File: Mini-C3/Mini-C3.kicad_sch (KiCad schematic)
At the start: 9 parts, among them J1 TB_1X2, J2 Conn_01x03, J3 Conn_01x07, J4 Conn_01x02, SW1 SW_Push, U1 Driver Module, U2 ESP32-C3_SUPERMINI

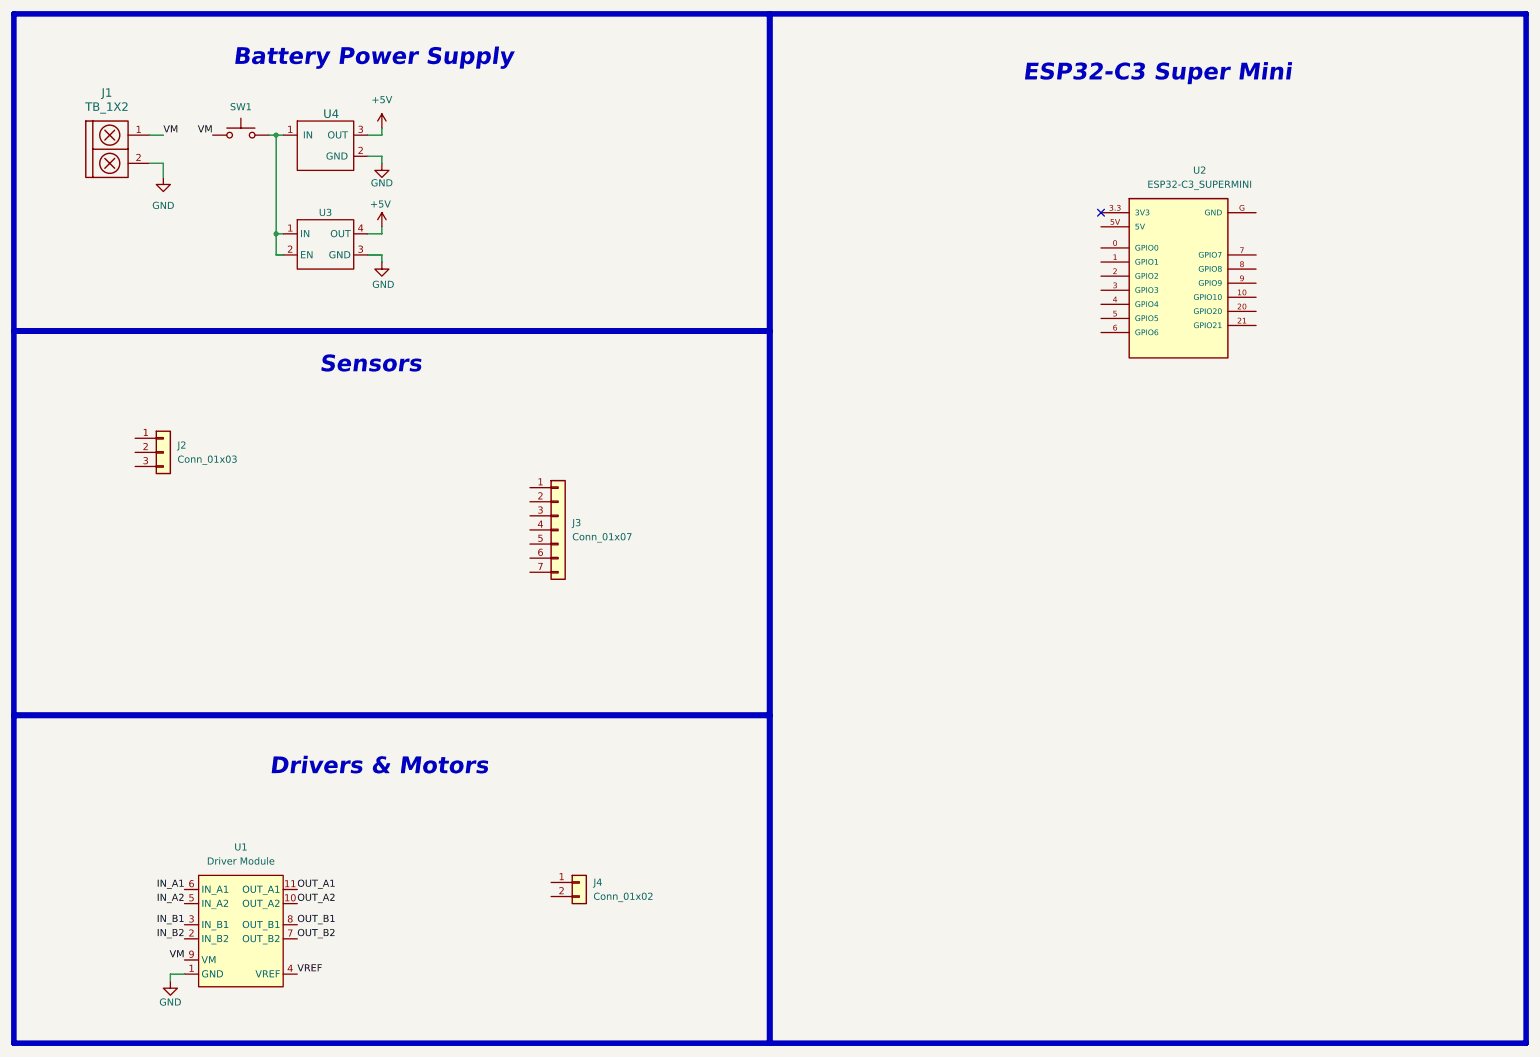
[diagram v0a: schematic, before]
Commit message: schematic & pcb
ESP32-C3 pinout img added. The schematic is almost done.
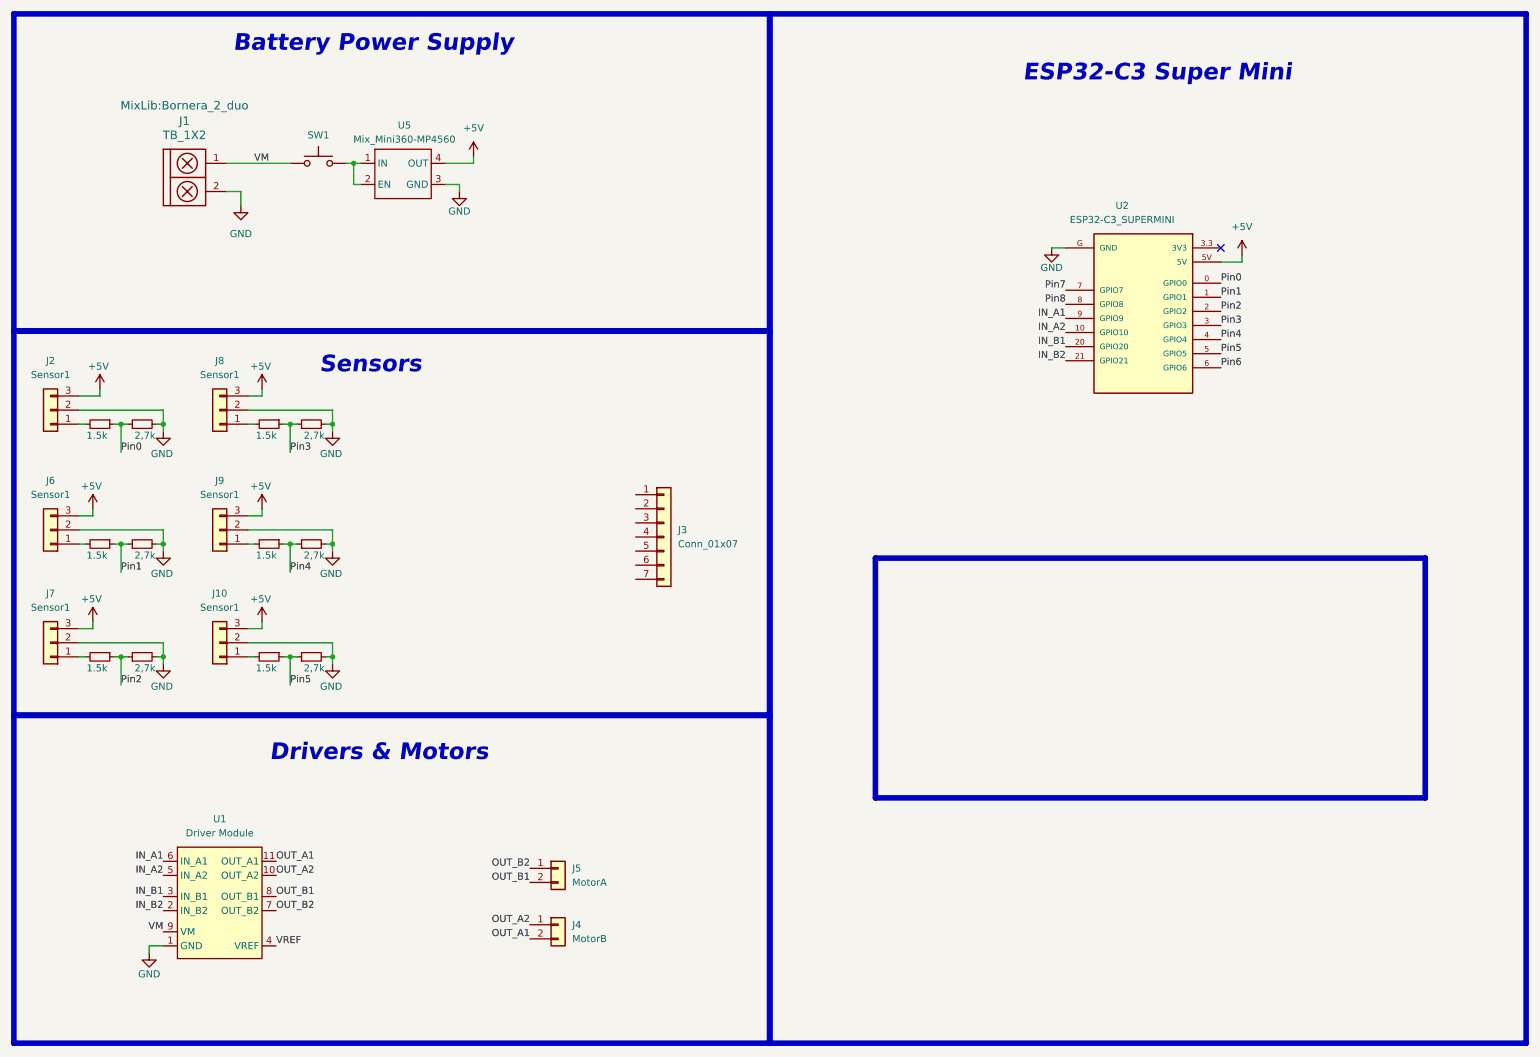
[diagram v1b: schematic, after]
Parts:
- removed U3: ~, MixLib:MP4560_Module, symbol MixLib:MP4560_Module
- removed U4: ~, MixLib:Mini360_step-down, symbol MixLib:Mini360
- added J10, J6, J7, J8, J9: Sensor1, MixLib:PinHeader_1x03_P2.54-SMD,THT,2-layers, symbol Connector_Generic:Conn_01x03
- added J5: MotorA, MixLib:Bornera_2_duo, symbol Connector_Generic:Conn_01x02
- added R1, R11, R3, R5, R7, R9: 1.5k, Resistor_SMD:R_0603_1608Metric, symbol Device:R_Small
- added R10, R12, R2, R4, R6, R8: 2,7k, Resistor_SMD:R_0603_1608Metric, symbol Device:R_Small
- added U5: Mix_Mini360-MP4560, MixLib:Mix_Mini360-MP4560, symbol MixLib:Mix_Mini360-MP4560
- J1: footprint (none) -> MixLib:Bornera_2_duo
- J2: value Conn_01x03 -> Sensor1; footprint (none) -> MixLib:PinHeader_1x03_P2.54-SMD,THT,2-layers
- J4: value Conn_01x02 -> MotorB; footprint (none) -> MixLib:Bornera_2_duo
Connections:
- net +5V: now also J2.3 (Pin_3), U2.5V, J10.3 (Pin_3), J6.3 (Pin_3), J7.3 (Pin_3), J8.3 (Pin_3), J9.3 (Pin_3), U5.4 (OUT)
- net GND: now also J2.2 (Pin_2), U2.G (GND), J10.2 (Pin_2), J6.2 (Pin_2), J7.2 (Pin_2), J8.2 (Pin_2), J9.2 (Pin_2), R10.2, R12.2, R2.2, R4.2, R6.2, R8.2, U5.3 (GND)
- net IN_A1: now also U2.9 (GPIO9)
- net IN_A2: now also U2.10 (GPIO10)
- net IN_B1: now also U2.20 (GPIO20)
- net IN_B2: now also U2.21 (GPIO21)
- net OUT_A1: now also J4.2 (Pin_2)
- net OUT_A2: now also J4.1 (Pin_1)
- net OUT_B1: now also J5.2 (Pin_2)
- net OUT_B2: now also J5.1 (Pin_1)
- net at SW1.2: now also U5.1 (IN), U5.2 (EN)
- net Pin0: now reaches U2.0 (GPIO0)
- net Pin0: now also R1.1, R2.1
- net Pin1: now reaches U2.1 (GPIO1)
- net Pin1: now also R3.1, R4.1
- net Pin2: now reaches U2.2 (GPIO2)
- net Pin2: now also R5.1, R6.1
- net Pin3: now reaches U2.3 (GPIO3)
- net Pin3: now also R7.1, R8.1
- net Pin4: now reaches U2.4 (GPIO4)
- net Pin4: now also R10.1, R9.1
- net Pin5: now reaches U2.5 (GPIO5)
- net Pin5: now also R11.1, R12.1
- net Pin6: now reaches U2.6 (GPIO6)
- net Pin7: now reaches U2.7 (GPIO7)
- net Pin8: now reaches U2.8 (GPIO8)
- net at J2.1 (Pin_1): now also R1.2
- new net: J10.1 (Pin_1), R11.2
- new net: J9.1 (Pin_1), R9.2
- new net: J6.1 (Pin_1), R3.2
- new net: J7.1 (Pin_1), R5.2
- new net: J8.1 (Pin_1), R7.2
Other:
- moved on the sheet: J1, J2, J3, J4, SW1, U1, U2

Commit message: PCB components placement
Improved the placement of the components.
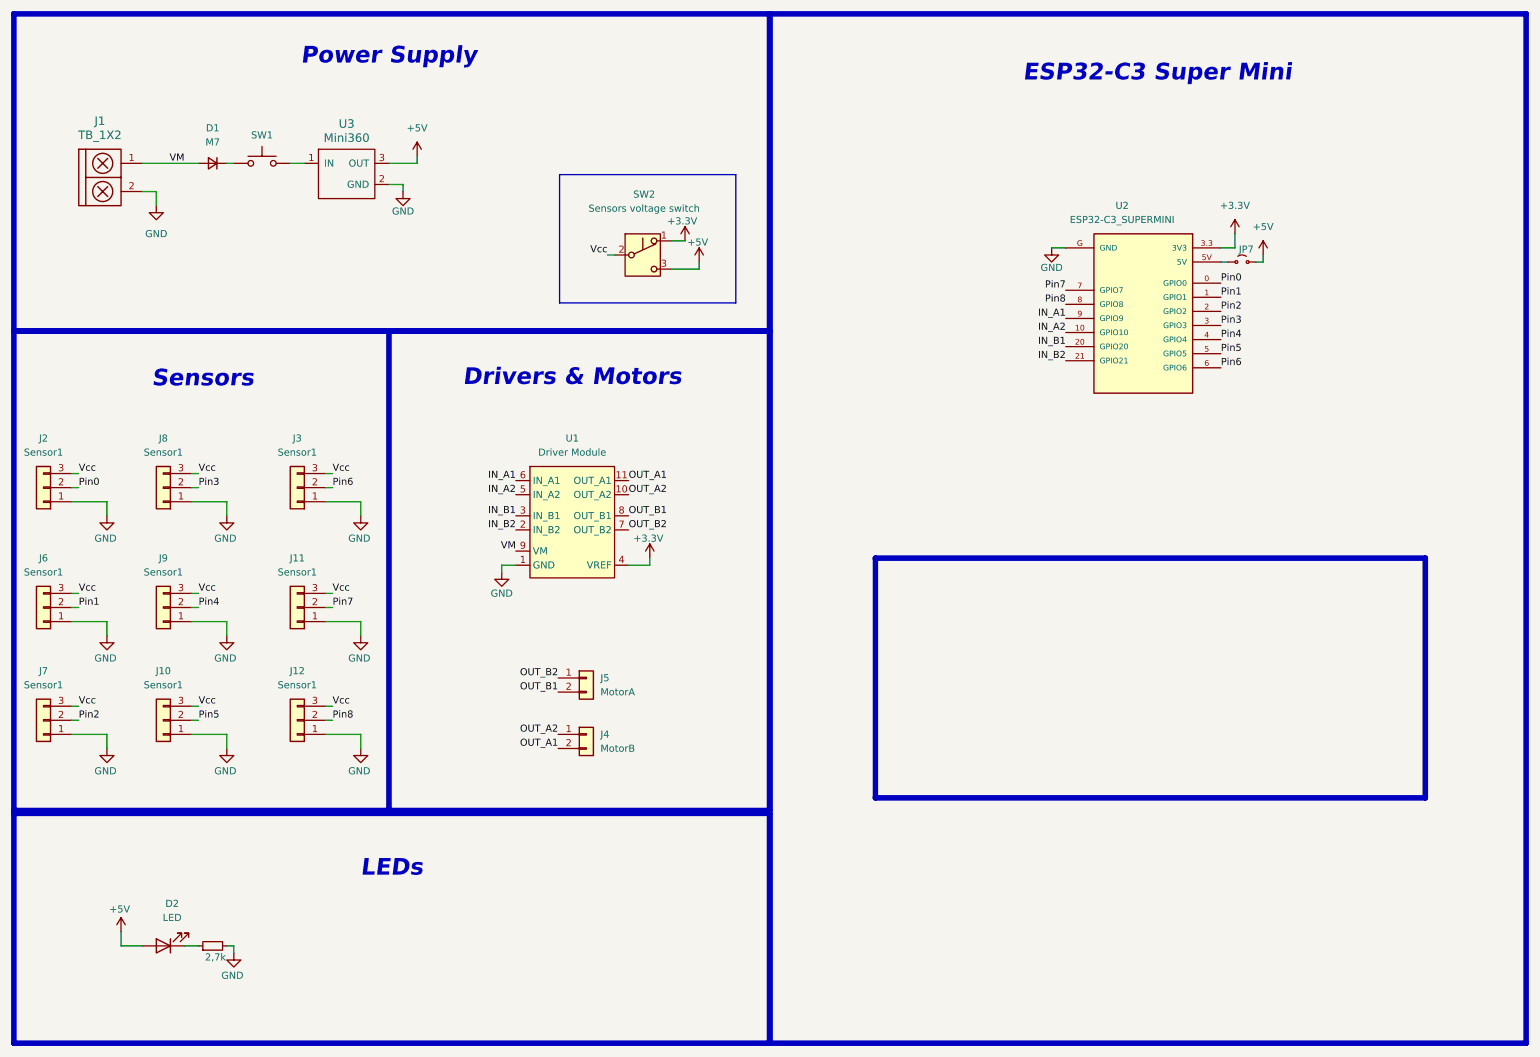
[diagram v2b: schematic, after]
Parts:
- removed J3: Conn_01x07, symbol Connector_Generic:Conn_01x07
- removed R1, R11, R3, R5, R7, R9: 1.5k, Resistor_SMD:R_0603_1608Metric, symbol Device:R_Small
- removed R10, R12, R2, R4, R6, R8: 2,7k, Resistor_SMD:R_0603_1608Metric, symbol Device:R_Small
- removed U5: Mix_Mini360-MP4560, MixLib:Mix_Mini360-MP4560, symbol MixLib:Mix_Mini360-MP4560
- added D1: M7, PCM_Diode_SMD_Handsoldering_AKL:D_SMA, symbol Device:D_Small
- added D2: LED, MixLib:LED_0805_2012Metric, symbol Device:LED
- added J11, J12, J3: Sensor1, MixLib:PinHeader_1x03_P2.54-THT, symbol Connector_Generic:Conn_01x03
- added JP7: Jumper_2_Small_Open, Jumper:SolderJumper-2_P1.3mm_Bridged_RoundedPad1.0x1.5mm, symbol Jumper:Jumper_2_Small_Open
- added R13: 2,7k, PCM_Resistor_SMD_AKL:R_0805_2012Metric, symbol Device:R_Small
- added SW2: Sensors voltage switch, MixLib:SW_Slide-03_P2.54_L9_W4_H7, symbol Switch:SW_Push_SPDT
- added U3: Mini360, MixLib:Mini360_step-down, symbol MixLib:Mini360
- J1, J4, J5: footprint MixLib:Bornera_2_duo -> Connector_Molex:Molex_KK-254_AE-6410-02A_1x02_P2.54mm_Vertical
- J10, J2, J6, J7, J8, J9: footprint MixLib:PinHeader_1x03_P2.54-SMD,THT,2-layers -> MixLib:PinHeader_1x03_P2.54-THT
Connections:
- net VREF is gone; now on net +3.3V: U1.4 (VREF)
- net +5V: now also D2.2 (A), JP7.2 (B), SW2.3 (C), U3.3 (OUT); no longer J10.3 (Pin_3), J2.3 (Pin_3), J6.3 (Pin_3), J7.3 (Pin_3), J8.3 (Pin_3), J9.3 (Pin_3), U2.5V
- net GND: now also J10.1 (Pin_1), J2.1 (Pin_1), J6.1 (Pin_1), J7.1 (Pin_1), J8.1 (Pin_1), J9.1 (Pin_1), J11.1 (Pin_1), J12.1 (Pin_1), J3.1 (Pin_1), R13.2, U3.2 (GND); no longer J10.2 (Pin_2), J2.2 (Pin_2), J6.2 (Pin_2), J7.2 (Pin_2), J8.2 (Pin_2), J9.2 (Pin_2)
- net Pin0: now also J2.2 (Pin_2)
- net Pin1: now also J6.2 (Pin_2)
- net Pin2: now also J7.2 (Pin_2)
- net Pin3: now also J8.2 (Pin_2)
- net Pin4: now also J9.2 (Pin_2)
- net Pin5: now also J10.2 (Pin_2)
- net Pin6: now also J3.2 (Pin_2)
- net Pin7: now also J11.2 (Pin_2)
- net Pin8: now also J12.2 (Pin_2)
- net VM: now also D1.2 (A); no longer SW1.1
- net at SW1.2: now also U3.1 (IN)
- net +3.3V: now reaches U2.3.3 (3V3)
- net +3.3V: now also SW2.1 (A)
- new net: D1.1 (K), SW1.1
- new net: D2.1 (K), R13.1
- new net: JP7.1 (A), U2.5V
- new net Vcc: J10.3 (Pin_3), J11.3 (Pin_3), J12.3 (Pin_3), J2.3 (Pin_3), J3.3 (Pin_3), J6.3 (Pin_3), J7.3 (Pin_3), J8.3 (Pin_3), J9.3 (Pin_3), SW2.2 (B)
- no-connect marks 1 -> 0
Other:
- note added: "LEDs"
- note added: "Power Supply"
- note removed: "Battery Power Supply"
- moved on the sheet: J1, J10, J2, J4, J5, J6, J7, J8, J9, SW1, U1

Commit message: pecebé
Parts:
- removed SW2: Sensors voltage switch, MixLib:SW_Slide-03_P2.54_L9_W4_H7, symbol Switch:SW_Push_SPDT
- added JP1: Sensors voltage jumper, Jumper:SolderJumper-3_P2.0mm_Open_TrianglePad1.0x1.5mm, symbol Jumper:Jumper_3_Open
- D2: footprint MixLib:LED_0805_2012Metric -> MixLib:LED_1206_3216Metric
- J1: footprint Connector_Molex:Molex_KK-254_AE-6410-02A_1x02_P2.54mm_Vertical -> MixLib:MyPinHeader-01x02-vertical
- J4, J5: footprint Connector_Molex:Molex_KK-254_AE-6410-02A_1x02_P2.54mm_Vertical -> MixLib:Bornera_2_duo
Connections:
- net +3.3V: now also JP1.1 (A)
- net +5V: now also JP1.3 (B); no longer D2.2 (A)
- net GND: now also J1.1; no longer J1.2
- net VM: now also J1.2; no longer J1.1
- net Vcc: now also D2.2 (A), JP1.2 (C)
- net at D1.1 (K): now also SW1.3; no longer SW1.1

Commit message: la pecebé
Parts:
- added R1: 100, PCM_Resistor_SMD_AKL:R_0805_2012Metric, symbol Device:R_Small
- added SW2: SW_Push, MixLib:SW_Slide-03_P2.54_L9_W4_H7, symbol EESTN5:SW_Push
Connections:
- net GND: now also J10.2 (Pin_2), J11.2 (Pin_2), J12.2 (Pin_2), J2.2 (Pin_2), J3.2 (Pin_2), J7.2 (Pin_2), J8.2 (Pin_2), J9.2 (Pin_2), U2.1 (GPIO1), R1.2; no longer J10.1 (Pin_1), J11.1 (Pin_1), J12.1 (Pin_1), J2.1 (Pin_1), J3.1 (Pin_1), J7.1 (Pin_1), J8.1 (Pin_1), J9.1 (Pin_1)
- net Pin0: now also J2.1 (Pin_1); no longer J2.2 (Pin_2)
- net Pin2: now also J7.1 (Pin_1); no longer J7.2 (Pin_2)
- net Pin3: now also J8.1 (Pin_1); no longer J8.2 (Pin_2)
- net Pin4: now also J9.1 (Pin_1); no longer J9.2 (Pin_2)
- net Pin5: now also J10.1 (Pin_1); no longer J10.2 (Pin_2)
- net Pin6: now also J3.1 (Pin_1), SW2.3; no longer J3.2 (Pin_2)
- net Pin7: now also J11.1 (Pin_1); no longer J11.2 (Pin_2)
- net Pin8: now also J12.1 (Pin_1); no longer J12.2 (Pin_2)
- net Pin1: no longer names the net of J6.2 (Pin_2)
- net Pin1: no longer U2.1 (GPIO1)
- new net: R1.1, SW2.2
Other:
- note added: "LEDs & Buttons"
- note removed: "LEDs"

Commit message: PCB almost there
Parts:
- added R2: 100, Resistor_SMD:R_0805_2012Metric, symbol Device:R_Small
- added SW3: SW_DIP_x02, Button_Switch_SMD:SW_DIP_SPSTx02_Slide_6.7x6.64mm_W8.61mm_P2.54mm_LowProfile, symbol Switch:SW_DIP_x02
- D2: footprint MixLib:LED_1206_3216Metric -> MixLib:LED_0805_2012Metric
- JP7: footprint Jumper:SolderJumper-2_P1.3mm_Bridged_RoundedPad1.0x1.5mm -> Jumper:SolderJumper-2_P1.3mm_Open_RoundedPad1.0x1.5mm
- R1, R13: footprint PCM_Resistor_SMD_AKL:R_0805_2012Metric -> Resistor_SMD:R_0805_2012Metric
- SW2: footprint MixLib:SW_Slide-03_P2.54_L9_W4_H7 -> Button_Switch_SMD:SW_Tactile_SPST_NO_Straight_CK_PTS636Sx25SMTRLFS
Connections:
- net GND: now also J10.1 (Pin_1), J11.1 (Pin_1), J12.1 (Pin_1), J2.1 (Pin_1), J3.1 (Pin_1), J7.1 (Pin_1), J8.1 (Pin_1), J9.1 (Pin_1), R2.1; no longer J10.2 (Pin_2), J11.2 (Pin_2), J12.2 (Pin_2), J2.2 (Pin_2), J3.2 (Pin_2), J7.2 (Pin_2), J8.2 (Pin_2), J9.2 (Pin_2), U2.1 (GPIO1)
- net IN_A1: now also U2.21 (GPIO21); no longer U2.9 (GPIO9)
- net IN_A2: now also U2.20 (GPIO20); no longer U2.10 (GPIO10)
- net IN_B1: now also U2.10 (GPIO10); no longer U2.20 (GPIO20)
- net IN_B2: now also U2.9 (GPIO9); no longer U2.21 (GPIO21)
- net Pin0: now also J10.2 (Pin_2); no longer J2.1 (Pin_1)
- net Pin2: now also J7.2 (Pin_2); no longer J7.1 (Pin_1)
- net Pin3: now also J8.2 (Pin_2); no longer J8.1 (Pin_1)
- net Pin4: now also J9.2 (Pin_2); no longer J9.1 (Pin_1)
- net Pin5: now also J2.2 (Pin_2); no longer J10.1 (Pin_1)
- net Pin6: now also J3.2 (Pin_2), SW3.1; no longer J3.1 (Pin_1), SW2.3
- net Pin7: now also J11.2 (Pin_2), SW2.1; no longer J11.1 (Pin_1)
- net Pin8: now also J12.2 (Pin_2), SW3.2; no longer J12.1 (Pin_1)
- net at U3.1 (IN): now also SW1.1; no longer SW1.2
- net at D1.1 (K): now also SW1.2; no longer SW1.3
- net Pin1: now reaches J6.2 (Pin_2)
- net Pin1: now also U2.1 (GPIO1)
- new net: R2.2, SW3.3, SW3.4
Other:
- moved on the sheet: D2, SW2

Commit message: Repositioned & added footprints
Honestly there's so much that was done that I just can't put it all here, also maybe because I don't remember. You should see the changes for yourself. Who reads these anyway?
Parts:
- added C1: 100uF, Capacitor_THT:C_Disc_D4.3mm_W1.9mm_P5.00mm, symbol Device:C_Small
- added H1, H2, H3: MountingHole_Pad, MountingHole:MountingHole_2.2mm_M2_DIN965_Pad, symbol Mechanical:MountingHole_Pad
- D1: footprint PCM_Diode_SMD_Handsoldering_AKL:D_SMA -> Diode_SMD:D_SMA
- J4, J5: footprint MixLib:Bornera_2_duo -> MixLib:MyPinHeader-01x02
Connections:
- net GND: now also C1.2
- net Pin7: now also J12.2 (Pin_2), SW3.2; no longer J11.2 (Pin_2), SW2.1
- net Pin8: now also J11.2 (Pin_2), SW2.1; no longer J12.2 (Pin_2), SW3.2
- net VM: now also C1.1
- no-connect marks 0 -> 3
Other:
- moved on the sheet: J4, J5
